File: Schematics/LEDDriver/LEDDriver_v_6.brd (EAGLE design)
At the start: 29.4 x 32.8 mm, 9 parts, among them IC1 CAT4101, IC2 CAT4101

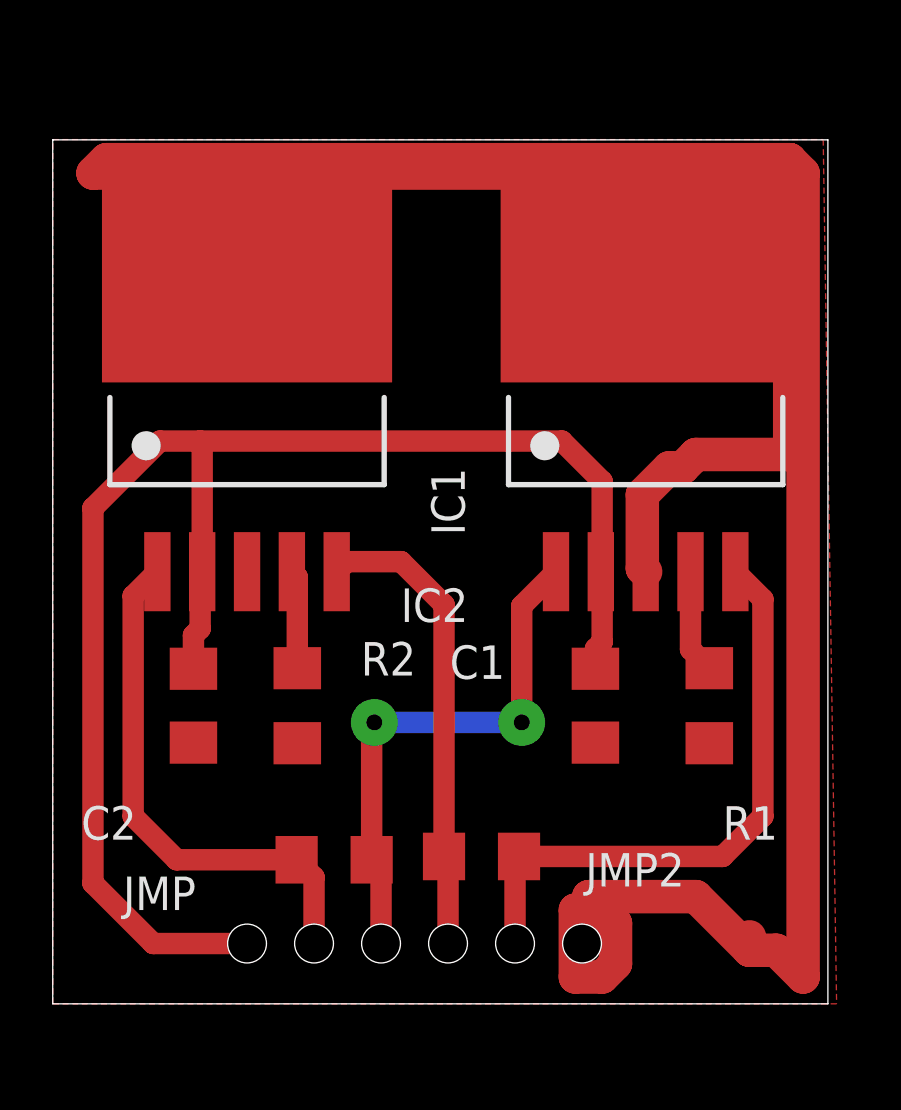
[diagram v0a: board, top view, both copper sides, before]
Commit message: Adding v6  LED driver schematic and web app
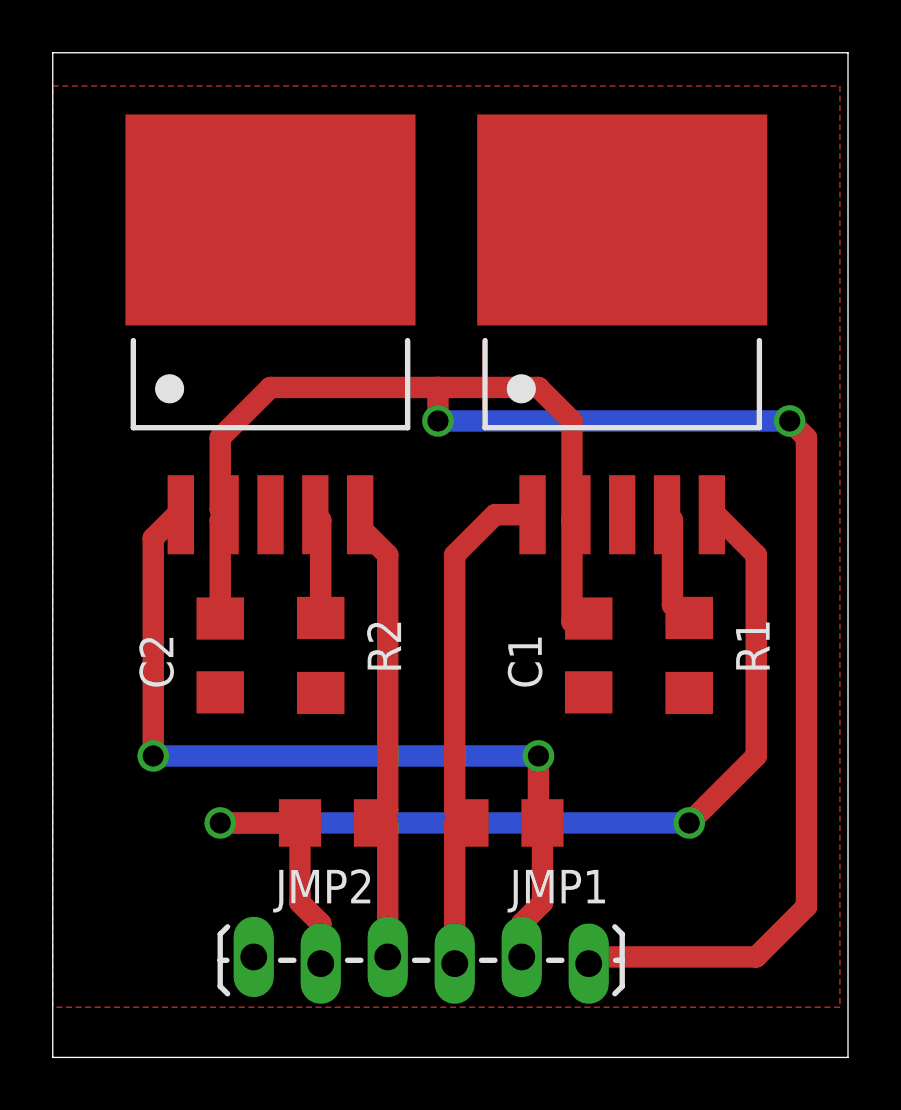
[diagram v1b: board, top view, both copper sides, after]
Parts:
- removed JMP: CH, adafruit:R1206
- added JMP1: CH, adafruit:R1206
- JP1: device SparkFun-Connectors:1X06_HOLES_ONLY -> SparkFun-Connectors:1X06_LOCK_LONGPADS
- moved JP1 12.5 mm to (7.62, 3.81), turned to 0 degrees
- moved JMP2 5.61 mm to (10.8, 8.89), turned to 180 degrees
- moved IC2 2.33 mm to (8.26, 28.6)
- moved IC1 2.33 mm to (21.6, 28.6)
- moved C2 2.16 mm to (6.35, 15.2)
- moved R2 2.10 mm to (10.2, 15.2)
- moved R1 2.05 mm to (24.1, 15.2)
- moved C1 1.92 mm to (20.3, 15.2)
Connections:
- net N$1: now also JMP1.2; no longer JMP.2
- net N$2: now also JMP1.1; no longer JMP.1
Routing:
- net GND: track 123.7 -> 0.00 mm
- net N$5: track 22.9 -> 40.0 mm, vias 0 -> 2
- net +5V: track 58.1 -> 72.7 mm, vias 0 -> 2
- net N$2: track 20.0 -> 32.3 mm, vias 0 -> 2
- net N$4: track 18.1 -> 17.4 mm
- net N$1: track 20.4 -> 19.8 mm, vias 2 -> 0
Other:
- board size 29.4 x 32.8 mm -> 30.1 x 38.1 mm
